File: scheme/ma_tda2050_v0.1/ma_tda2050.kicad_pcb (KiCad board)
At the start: 2 copper layers, 104 x 42 mm, 44 parts, among them J1 Power, J2 Input, J3 Out_L, J4 Out_R, U1 TDA2050, U2 TDA2050

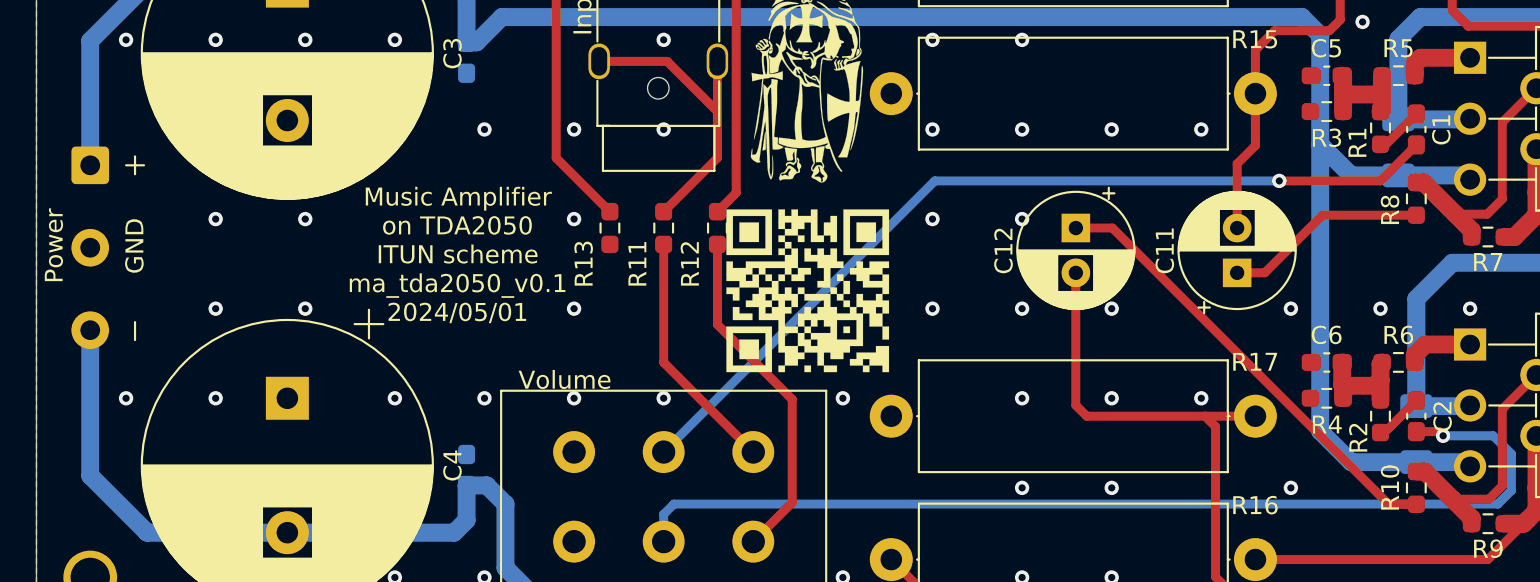
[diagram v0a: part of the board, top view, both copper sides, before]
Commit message: small: QR code
Change QR code from github to site.
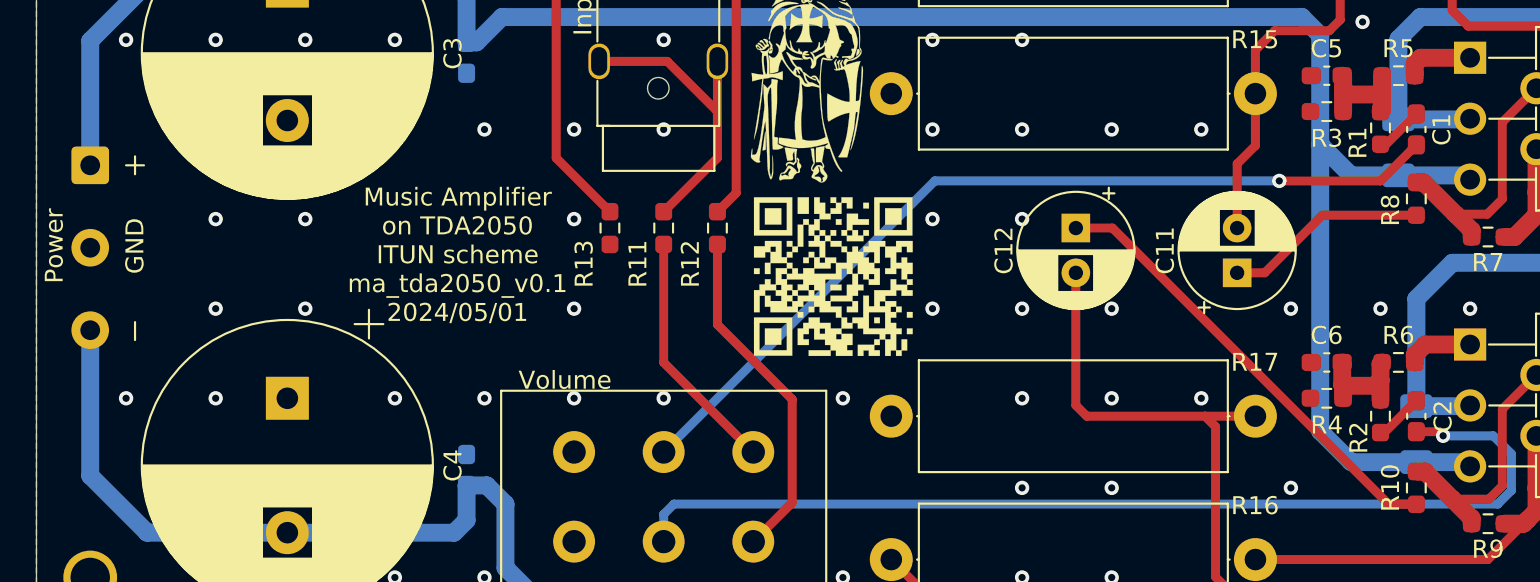
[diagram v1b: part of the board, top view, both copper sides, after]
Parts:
- removed the G*** at (123.0, 109.0)
- added G***: LOGO, mine:qr_code, F.Cu at (124.5, 108.2)
